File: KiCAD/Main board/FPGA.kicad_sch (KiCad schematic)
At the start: 1 part

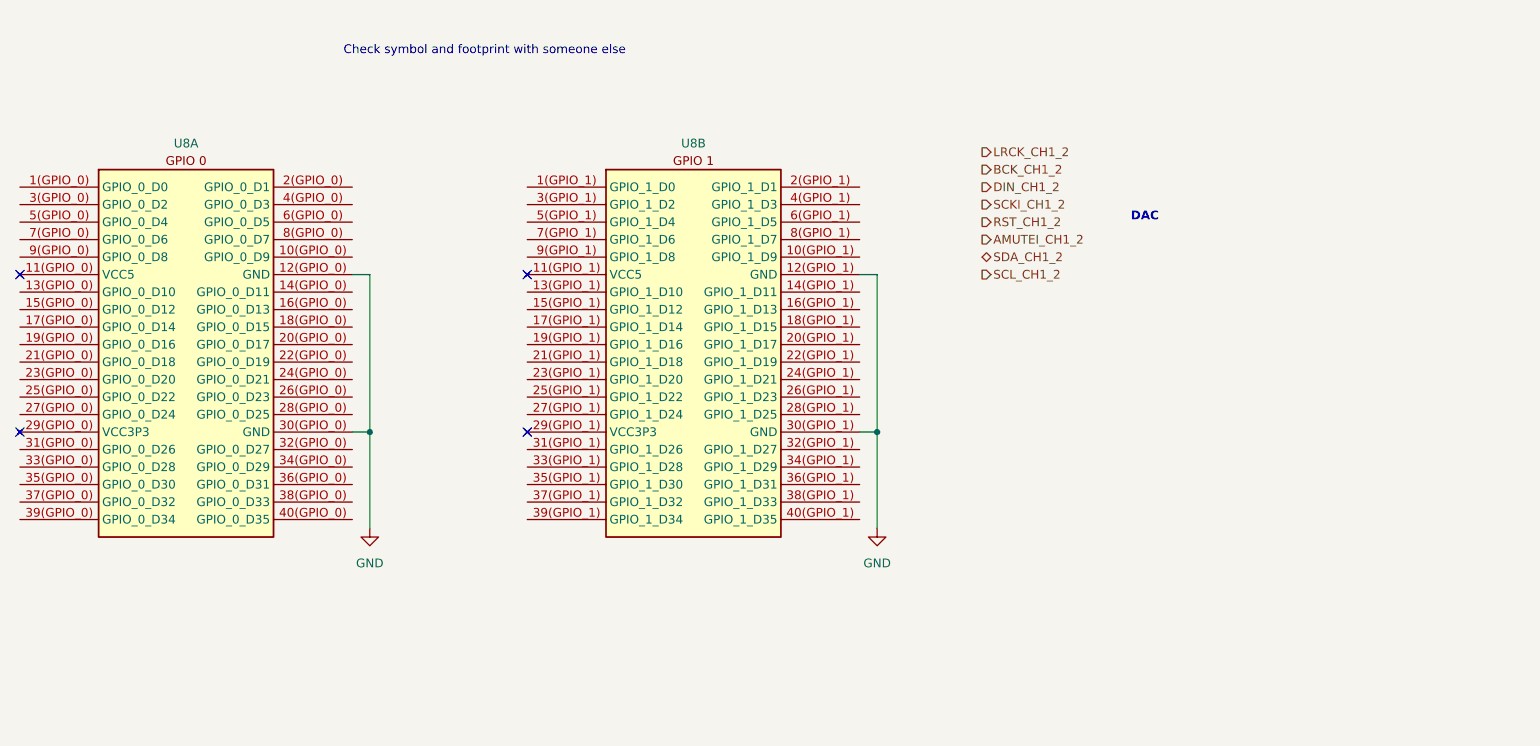
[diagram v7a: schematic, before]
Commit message: Worked on main board schematic and PCB, added symbols to symbol library
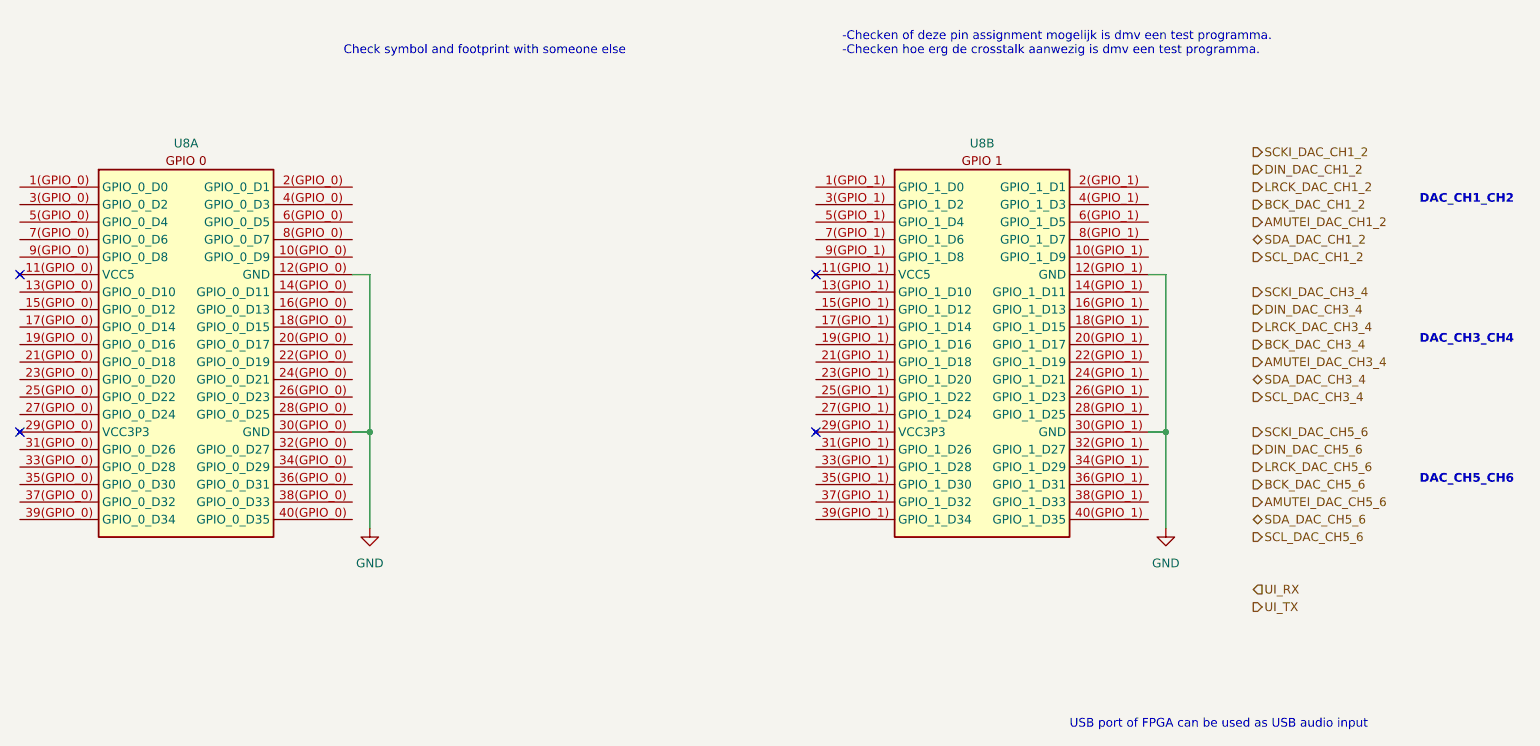
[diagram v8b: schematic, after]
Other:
- note added: "-Checken of deze pin assignment mogelijk is dmv een test programma. -Checken hoe erg de crosstalk aanwezig is dmv een test programma."
- note added: "DAC_CH1_CH2"
- note added: "DAC_CH3_CH4"
- note added: "DAC_CH5_CH6"
- note added: "USB port of FPGA can be used as USB audio input"
- note removed: "DAC"
- moved on the sheet: U8B
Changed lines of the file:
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@@
 (kicad_sch (version 20230121) (generator eeschema)
   (paper "A4")
-  (junction (at 153.67 90.17) (diameter 0) (color 0 0 0 0)
+  (junction (at 195.58 90.17) (diameter 0) (color 0 0 0 0)
   )
   (junction (at 80.01 90.17) (diameter 0) (color 0 0 0 0)
   )
   (no_connect (at 29.21 90.17))
-  (no_connect (at 102.87 67.31))
+  (no_connect (at 144.78 67.31))
   (no_connect (at 29.21 67.31))
-  (no_connect (at 102.87 90.17))
-  (wire (pts (xy 151.13 67.31) (xy 153.67 67.31))
+  (no_connect (at 144.78 90.17))
+  (wire (pts (xy 193.04 67.31) (xy 195.58 67.31))
     (stroke (width 0) (type default))
   )
@@
     (stroke (width 0) (type default))
   )
-  (wire (pts (xy 153.67 67.31) (xy 153.67 90.17))
+  (wire (pts (xy 195.58 67.31) (xy 195.58 90.17))
     (stroke (width 0) (type default))
   )
@@
     (stroke (width 0) (type default))
   )
-  (wire (pts (xy 153.67 104.14) (xy 153.67 90.17))
+  (wire (pts (xy 195.58 104.14) (xy 195.58 90.17))
     (stroke (width 0) (type default))
   )
@@
     (stroke (width 0) (type default))
   )
-  (wire (pts (xy 151.13 90.17) (xy 153.67 90.17))
-    (stroke (width 0) (type default))
-  )
-  (text "DAC" (at 190.5 59.69 0)
+  (wire (pts (xy 193.04 90.17) (xy 195.58 90.17))
+    (stroke (width 0) (type default))
+  )
+  (text "-Checken of deze pin assignment mogelijk is dmv een test programma.\n-Checken hoe erg de crosstalk aanwezig is dmv een test programma.\n"
+    (at 148.59 35.56 0)
+    (effects (font (size 1.27 1.27) (color 200 0 200 1)) (justify left bottom))
+  )
+  (text "DAC_CH1_CH2" (at 232.41 57.15 0)
     (effects (font (size 1.27 1.27) bold) (justify left bottom))
   )
+  (text "USB port of FPGA can be used as USB audio input" (at 181.61 133.35 0)
+    (effects (font (size 1.27 1.27)) (justify left bottom))
+  )
   (text "Check symbol and footprint with someone else" (at 76.2 35.56 0)
-    (effects (font (size 1.27 1.27) (color 255 0 0 1)) (justify left bottom))
-  )
-  (hierarchical_label "RST_CH1_2" (shape output) (at 168.91 59.69 0) (fields_autoplaced)
-    (effects (font (size 1.27 1.27)) (justify left))
-  )
-  (hierarchical_label "DIN_CH1_2" (shape output) (at 168.91 54.61 0) (fields_autoplaced)
-    (effects (font (size 1.27 1.27)) (justify left))
-  )
-  (hierarchical_label "SCL_CH1_2" (shape output) (at 168.91 67.31 0) (fields_autoplaced)
-    (effects (font (size 1.27 1.27)) (justify left))
-  )
-  (hierarchical_label "BCK_CH1_2" (shape output) (at 168.91 52.07 0) (fields_autoplaced)
-    (effects (font (size 1.27 1.27)) (justify left))
-  )
-  (hierarchical_label "SDA_CH1_2" (shape bidirectional) (at 168.91 64.77 0) (fields_autoplaced)
-    (effects (font (size 1.27 1.27)) (justify left))
-  )
-  (hierarchical_label "AMUTEI_CH1_2" (shape output) (at 168.91 62.23 0) (fields_autoplaced)
-    (effects (font (size 1.27 1.27)) (justify left))
-  )
-  (hierarchical_label "LRCK_CH1_2" (shape output) (at 168.91 49.53 0) (fields_autoplaced)
-    (effects (font (size 1.27 1.27)) (justify left))
-  )
-  (hierarchical_label "SCKI_CH1_2" (shape output) (at 168.91 57.15 0) (fields_autoplaced)
+    (effects (font (size 1.27 1.27) (color 200 0 200 1)) (justify left bottom))
+  )
+  (text "DAC_CH3_CH4" (at 232.41 77.47 0)
+    (effects (font (size 1.27 1.27) bold) (justify left bottom))
+  )
+  (text "DAC_CH5_CH6" (at 232.41 97.79 0)
+    (effects (font (size 1.27 1.27) bold) (justify left bottom))
+  )
+  (hierarchical_label "AMUTEI_DAC_CH5_6" (shape output) (at 208.28 100.33 0) (fields_autoplaced)
+    (effects (font (size 1.27 1.27)) (justify left))
+  )
+  (hierarchical_label "UI_TX" (shape output) (at 208.28 115.57 0) (fields_autoplaced)
+    (effects (font (size 1.27 1.27)) (justify left))
+  )
+  (hierarchical_label "DIN_DAC_CH3_4" (shape output) (at 208.28 72.39 0) (fields_autoplaced)
+    (effects (font (size 1.27 1.27)) (justify left))
+  )
+  (hierarchical_label "SCL_DAC_CH5_6" (shape output) (at 208.28 105.41 0) (fields_autoplaced)
+    (effects (font (size 1.27 1.27)) (justify left))
+  )
+  (hierarchical_label "LRCK_DAC_CH1_2" (shape output) (at 208.28 54.61 0) (fields_autoplaced)
+    (effects (font (size 1.27 1.27)) (justify left))
+  )
+  (hierarchical_label "SCL_DAC_CH1_2" (shape output) (at 208.28 64.77 0) (fields_autoplaced)
+    (effects (font (size 1.27 1.27)) (justify left))
+  )
+  (hierarchical_label "LRCK_DAC_CH5_6" (shape output) (at 208.28 95.25 0) (fields_autoplaced)
+    (effects (font (size 1.27 1.27)) (justify left))
+  )
+  (hierarchical_label "DIN_DAC_CH1_2" (shape output) (at 208.28 52.07 0) (fields_autoplaced)
+    (effects (font (size 1.27 1.27)) (justify left))
+  )
+  (hierarchical_label "SCKI_DAC_CH3_4" (shape output) (at 208.28 69.85 0) (fields_autoplaced)
+    (effects (font (size 1.27 1.27)) (justify left))
+  )
+  (hierarchical_label "AMUTEI_DAC_CH3_4" (shape output) (at 208.28 80.01 0) (fields_autoplaced)
+    (effects (font (size 1.27 1.27)) (justify left))
+  )
+  (hierarchical_label "UI_RX" (shape input) (at 208.28 113.03 0) (fields_autoplaced)
+    (effects (font (size 1.27 1.27)) (justify left))
+  )
+  (hierarchical_label "SCL_DAC_CH3_4" (shape output) (at 208.28 85.09 0) (fields_autoplaced)
+    (effects (font (size 1.27 1.27)) (justify left))
+  )
+  (hierarchical_label "DIN_DAC_CH5_6" (shape output) (at 208.28 92.71 0) (fields_autoplaced)
+    (effects (font (size 1.27 1.27)) (justify left))
+  )
+  (hierarchical_label "SDA_DAC_CH1_2" (shape bidirectional) (at 208.28 62.23 0) (fields_autoplaced)
+    (effects (font (size 1.27 1.27)) (justify left))
+  )
+  (hierarchical_label "AMUTEI_DAC_CH1_2" (shape output) (at 208.28 59.69 0) (fields_autoplaced)
+    (effects (font (size 1.27 1.27)) (justify left))
+  )
+  (hierarchical_label "BCK_DAC_CH5_6" (shape output) (at 208.28 97.79 0) (fields_autoplaced)
+    (effects (font (size 1.27 1.27)) (justify left))
+  )
+  (hierarchical_label "SDA_DAC_CH3_4" (shape bidirectional) (at 208.28 82.55 0) (fields_autoplaced)
+    (effects (font (size 1.27 1.27)) (justify left))
+  )
+  (hierarchical_label "BCK_DAC_CH3_4" (shape output) (at 208.28 77.47 0) (fields_autoplaced)
+    (effects (font (size 1.27 1.27)) (justify left))
+  )
+  (hierarchical_label "SCKI_DAC_CH1_2" (shape output) (at 208.28 49.53 0) (fields_autoplaced)
+    (effects (font (size 1.27 1.27)) (justify left))
+  )
+  (hierarchical_label "LRCK_DAC_CH3_4" (shape output) (at 208.28 74.93 0) (fields_autoplaced)
+    (effects (font (size 1.27 1.27)) (justify left))
+  )
+  (hierarchical_label "SCKI_DAC_CH5_6" (shape output) (at 208.28 90.17 0) (fields_autoplaced)
+    (effects (font (size 1.27 1.27)) (justify left))
+  )
+  (hierarchical_label "BCK_DAC_CH1_2" (shape output) (at 208.28 57.15 0) (fields_autoplaced)
+    (effects (font (size 1.27 1.27)) (justify left))
+  )
+  (hierarchical_label "SDA_DAC_CH5_6" (shape bidirectional) (at 208.28 102.87 0) (fields_autoplaced)
     (effects (font (size 1.27 1.27)) (justify left))
   )
@@
     )
   )
-  (symbol (lib_id "Audio_DSP:DE1-SoC") (at 127 77.47 0) (unit 2)
+  (symbol (lib_id "Audio_DSP:DE1-SoC") (at 168.91 77.47 0) (unit 2)
     (in_bom yes) (on_board yes) (dnp no) (fields_autoplaced)
-    (property "Reference" "U8" (at 127 48.26 0)
-      (effects (font (size 1.27 1.27)))
-    )
-    (property "Value" "~" (at 127 77.47 0)
-      (effects (font (size 1.27 1.27)))
-    )
-    (property "Footprint" "Audio-DSP:DE1-SoC" (at 127 77.47 0)
-      (effects (font (size 1.27 1.27)) hide)
-    )
-    (property "Datasheet" "NA" (at 127 77.47 0)
+    (property "Reference" "U8" (at 168.91 48.26 0)
+      (effects (font (size 1.27 1.27)))
+    )
+    (property "Value" "~" (at 168.91 77.47 0)
+      (effects (font (size 1.27 1.27)))
+    )
+    (property "Footprint" "Audio-DSP:DE1-SoC" (at 168.91 77.47 0)
+      (effects (font (size 1.27 1.27)) hide)
+    )
+    (property "Datasheet" "NA" (at 168.91 77.47 0)
       (effects (font (size 1.27 1.27)) hide)
     )
@@
     )
   )
-  (symbol (lib_id "power:GND") (at 153.67 104.14 0) (unit 1)
+  (symbol (lib_id "power:GND") (at 195.58 104.14 0) (unit 1)
     (in_bom yes) (on_board yes) (dnp no) (fields_autoplaced)
-    (property "Reference" "#PWR0170" (at 153.67 110.49 0)
-      (effects (font (size 1.27 1.27)) hide)
-    )
-    (property "Value" "GND" (at 153.67 109.22 0)
-      (effects (font (size 1.27 1.27)))
-    )
-    (property "Footprint" "" (at 153.67 104.14 0)
-      (effects (font (size 1.27 1.27)) hide)
-    )
-    (property "Datasheet" "" (at 153.67 104.14 0)
-      (effects (font (size 1.27 1.27)) hide)
-    )
+    (property "Reference" "#PWR0170" (at 195.58 110.49 0)
+      (effects (font (size 1.27 1.27)) hide)
+    )
+    (property "Value" "GND" (at 195.58 109.22 0)
+      (effects (font (size 1.27 1.27)))
+    )
+    (property "Footprint" "" (at 195.58 104.14 0)
+      (effects (font (size 1.27 1.27)) hide)
+    )
+    (property "Datasheet" "" (at 195.58 104.14 0)
+      (effects (font (size 1.27 1.27)) hide)
+    )
